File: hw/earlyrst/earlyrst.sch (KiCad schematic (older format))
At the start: 13 parts

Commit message: comment about -pcLoad signal
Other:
- note added: "-pcLoad asserts the initial PC\nupper/lower byte value on the\nALU data bus, and also drives\nthe parallel load input on the\nPC register"
- note removed: "-pcLoad asserts the initial PC\nupper/lower byte value on the\nALU data bus"
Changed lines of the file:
@@
 	1    0    0    -1
 $EndComp
-Text Notes 9700 1350 0    60   ~ 0
--pcLoad asserts the initial PC\nupper/lower byte value on the\nALU data bus
+Text Notes 9550 1300 0    60   ~ 0
+-pcLoad asserts the initial PC\nupper/lower byte value on the\nALU data bus, and also drives\nthe parallel load input on the\nPC register
 Text Notes 9850 3150 0    60   ~ 0
 -lateRST is the active-low\nreset signal for all other\ndevices

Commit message: bugfix/redesign
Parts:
- removed U?: 74LS32, symbol 74LS32
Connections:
- wire segments 83 -> 77
- no-connect marks 8 -> 7
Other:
- note added: "-lateRST is the\nactive-low reset\nsignal for all other\ndevices"
- note added: "-pcLoad asserts the initial PC\nupper/lower byte value on the\nALU data bus"
- note removed: "-lateRST is the active-low\nreset signal for all other\ndevices"
- note removed: "-pcLoad asserts the initial PC\nupper/lower byte value on the\nALU data bus, and also drives\nthe parallel load input on the\nPC register"
- moved on the sheet: U?, U?A, U?B, U?C, U?D
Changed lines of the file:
@@
 L 74LS32 U?
 U 1 1 592592CC
-P 5850 2600
-F 0 "U?" H 5850 2650 50  0000 C CNN
-F 1 "74LS32" H 5850 2550 50  0000 C CNN
-F 2 "" H 5850 2600 50  0001 C CNN
-F 3 "" H 5850 2600 50  0001 C CNN
-	1    5850 2600
+P 6750 2600
+F 0 "U?" H 6750 2650 50  0000 C CNN
+F 1 "74LS32" H 6750 2550 50  0000 C CNN
+F 2 "" H 6750 2600 50  0001 C CNN
+F 3 "" H 6750 2600 50  0001 C CNN
+	1    6750 2600
 	1    0    0    -1
 $EndComp
@@
 L 74LS04 U?
 U 3 1 59259341
-P 7050 2600
-F 0 "U?" H 7245 2715 50  0000 C CNN
-F 1 "74LS04" H 7240 2475 50  0000 C CNN
-F 2 "" H 7050 2600 50  0001 C CNN
-F 3 "" H 7050 2600 50  0001 C CNN
-	3    7050 2600
+P 5550 2500
+F 0 "U?" H 5745 2615 50  0000 C CNN
+F 1 "74LS04" H 5740 2375 50  0000 C CNN
+F 2 "" H 5550 2500 50  0001 C CNN
+F 3 "" H 5550 2500 50  0001 C CNN
+	3    5550 2500
 	1    0    0    -1
 $EndComp
@@
 L 74LS175 U?
 U 1 1 59259407
-P 8350 3050
-F 0 "U?" H 8350 3050 50  0000 C CNN
-F 1 "74LS175" H 8450 2650 50  0000 C CNN
-F 2 "" H 8350 3050 50  0001 C CNN
-F 3 "" H 8350 3050 50  0001 C CNN
-	1    8350 3050
+P 8550 3050
+F 0 "U?" H 8550 3050 50  0000 C CNN
+F 1 "74LS175" H 8650 2650 50  0000 C CNN
+F 2 "" H 8550 3050 50  0001 C CNN
+F 3 "" H 8550 3050 50  0001 C CNN
+	1    8550 3050
 	1    0    0    -1
 $EndComp
@@
 L 74LS32 U?
 U 2 1 59259471
-P 5850 3350
-F 0 "U?" H 5850 3400 50  0000 C CNN
-F 1 "74LS32" H 5850 3300 50  0000 C CNN
-F 2 "" H 5850 3350 50  0001 C CNN
-F 3 "" H 5850 3350 50  0001 C CNN
-	2    5850 3350
-	1    0    0    -1
-$EndComp
-Text Label 4650 2500 0    60   ~ 0
-CT0
-Text Label 4650 2600 0    60   ~ 0
-CT1
-Text Label 9900 2800 0    60   ~ 0
+P 6750 3100
+F 0 "U?" H 6750 3150 50  0000 C CNN
+F 1 "74LS32" H 6750 3050 50  0000 C CNN
+F 2 "" H 6750 3100 50  0001 C CNN
+F 3 "" H 6750 3100 50  0001 C CNN
+	2    6750 3100
+	1    0    0    -1
+$EndComp
+Text Label 10100 2800 0    60   ~ 0
 -lateRST
 $Comp
 L GND #PWR?
 U 1 1 59259887
-P 6800 3500
-F 0 "#PWR?" H 6800 3250 50  0001 C CNN
-F 1 "GND" H 6800 3350 50  0000 C CNN
-F 2 "" H 6800 3500 50  0001 C CNN
-F 3 "" H 6800 3500 50  0001 C CNN
-	1    6800 3500
+P 7700 4500
+F 0 "#PWR?" H 7700 4250 50  0001 C CNN
+F 1 "GND" H 7700 4350 50  0000 C CNN
+F 2 "" H 7700 4500 50  0001 C CNN
+F 3 "" H 7700 4500 50  0001 C CNN
+	1    7700 4500
 	1    0    0    -1
 $EndComp
@@
 $Comp
 L 74LS32 U?
-U 3 1 59259CFD
-P 10050 1600
-F 0 "U?" H 10050 1650 50  0000 C CNN
-F 1 "74LS32" H 10050 1550 50  0000 C CNN
-F 2 "" H 10050 1600 50  0001 C CNN
-F 3 "" H 10050 1600 50  0001 C CNN
-	3    10050 1600
-	1    0    0    -1
-$EndComp
-Text Label 10700 1600 0    60   ~ 0
--pcLoad
-$Comp
-L 74LS32 U?
 U 4 1 5925A3F5
 P 2900 5500
@@
 L 74LS04 U?
 U 4 1 5925A468
-P 2750 5950
-F 0 "U?" H 2945 6065 50  0000 C CNN
-F 1 "74LS04" H 2940 5825 50  0000 C CNN
-F 2 "" H 2750 5950 50  0001 C CNN
-F 3 "" H 2750 5950 50  0001 C CNN
-	4    2750 5950
+P 5550 3000
+F 0 "U?" H 5745 3115 50  0000 C CNN
+F 1 "74LS04" H 5740 2875 50  0000 C CNN
+F 2 "" H 5550 3000 50  0001 C CNN
+F 3 "" H 5550 3000 50  0001 C CNN
+	4    5550 3000
 	1    0    0    -1
 $EndComp
@@
 	1    0    0    -1
 $EndComp
-Text Notes 9550 1300 0    60   ~ 0
--pcLoad asserts the initial PC\nupper/lower byte value on the\nALU data bus, and also drives\nthe parallel load input on the\nPC register
-Text Notes 9850 3150 0    60   ~ 0
--lateRST is the active-low\nreset signal for all other\ndevices
+Text Notes 10050 3250 0    60   ~ 0
+-lateRST is the\nactive-low reset\nsignal for all other\ndevices
 $Comp
 L GND #PWR?
@@
 $EndComp
 NoConn ~ 3750 5500
-NoConn ~ 3750 5950
 NoConn ~ 3750 6300
 NoConn ~ 3750 6650
@@
 	4600 2700 4900 2700
 Wire Wire Line
-	6600 2600 6450 2600
-Wire Wire Line
-	5250 2700 5100 2700
-Wire Wire Line
-	5100 2600 5100 3250
-Wire Wire Line
-	5100 3250 5250 3250
-Connection ~ 5100 2700
-Wire Wire Line
-	4600 2500 5250 2500
-Wire Wire Line
-	4600 2600 5100 2600
-Wire Wire Line
-	7500 2600 7650 2600
-Wire Wire Line
-	9050 2800 10400 2800
-Wire Wire Line
-	5250 3450 5100 3450
-Wire Wire Line
-	5100 3450 5100 3850
-Wire Wire Line
-	5100 3850 9650 3850
-Wire Wire Line
-	9650 3850 9650 2800
-Connection ~ 9650 2800
-Wire Wire Line
-	7650 2800 7350 2800
-Wire Wire Line
-	7350 2800 7350 3350
-Wire Wire Line
-	7350 3350 6450 3350
-Wire Wire Line
-	7650 3000 6800 3000
-Wire Wire Line
-	6800 3000 6800 3500
-Wire Wire Line
-	7650 3200 6800 3200
-Connection ~ 6800 3200
-Wire Wire Line
-	7650 3500 7550 3500
-Wire Wire Line
-	7550 3500 7550 4300
-Wire Wire Line
-	7550 4300 750  4300
+	7350 2600 7850 2600
+Wire Wire Line
+	9250 2800 10600 2800
+Wire Wire Line
+	9850 3850 9850 2800
+Connection ~ 9850 2800
+Wire Wire Line
+	750  4300 7550 4300
 Connection ~ 750  3300
 Wire Wire Line
-	9300 1500 9300 2700
-Wire Wire Line
 	1000 1050 550  1050
 Wire Wire Line
 	750  1400 550  1400
 Wire Wire Line
-	7650 3400 7450 3400
-Wire Wire Line
-	7450 3400 7450 4150
-Wire Wire Line
-	7450 4150 1000 4150
+	1000 4150 7450 4150
 Connection ~ 1000 2950
-Wire Wire Line
-	9450 1700 9450 2800
-Connection ~ 9450 2800
-Wire Wire Line
-	9300 1500 9450 1500
-Wire Wire Line
-	10650 1600 11100 1600
 Wire Wire Line
 	2300 5400 1900 5400
@@
 Connection ~ 1900 5600
 Wire Wire Line
-	2300 5950 1900 5950
-Connection ~ 1900 5950
-Wire Wire Line
 	2300 6300 1900 6300
 Connection ~ 1900 6300
@@
 	3500 5500 3750 5500
 Wire Wire Line
-	3200 5950 3750 5950
-Wire Wire Line
 	3200 6300 3750 6300
 Wire Wire Line
 	3200 6650 3750 6650
-Wire Wire Line
-	9300 2700 9050 2700
 Wire Wire Line
 	6100 5600 4950 5600
@@
 Text Notes 6350 6300 0    60   ~ 0
 the initial PC value is\n0xC0C0
+Wire Wire Line
+	9250 2600 10600 2600
+Text Label 10100 2600 0    60   ~ 0
+-pcLoad
+Wire Wire Line
+	6150 2500 6000 2500
+Wire Wire Line
+	7850 3000 7700 3000
+Wire Wire Line
+	7700 3000 7700 4500
+Wire Wire Line
+	7850 3200 7700 3200
+Connection ~ 7700 3200
+Wire Wire Line
+	4600 2500 5100 2500
+Wire Wire Line
+	4600 2600 5100 2600
+Wire Wire Line
+	5100 2600 5100 3000
+Text Label 4600 2500 0    60   ~ 0
+CT0
+Text Label 4600 2600 0    60   ~ 0
+CT1
+Wire Wire Line
+	6000 3000 6150 3000
+Wire Wire Line
+	7850 3500 7550 3500
+Wire Wire Line
+	7550 3500 7550 4300
+Wire Wire Line
+	7850 3400 7450 3400
+Wire Wire Line
+	7450 3400 7450 4150
+Wire Wire Line
+	9850 3850 6050 3850
+Wire Wire Line
+	6050 3850 6050 2700
+Wire Wire Line
+	6050 2700 6150 2700
+Wire Wire Line
+	6150 3200 6050 3200
+Connection ~ 6050 3200
+Wire Wire Line
+	7350 3100 7500 3100
+Wire Wire Line
+	7500 3100 7500 2800
+Wire Wire Line
+	7500 2800 7850 2800
+Text Notes 9600 2450 0    60   ~ 0
+-pcLoad asserts the initial PC\nupper/lower byte value on the\nALU data bus
 $EndSCHEMATC

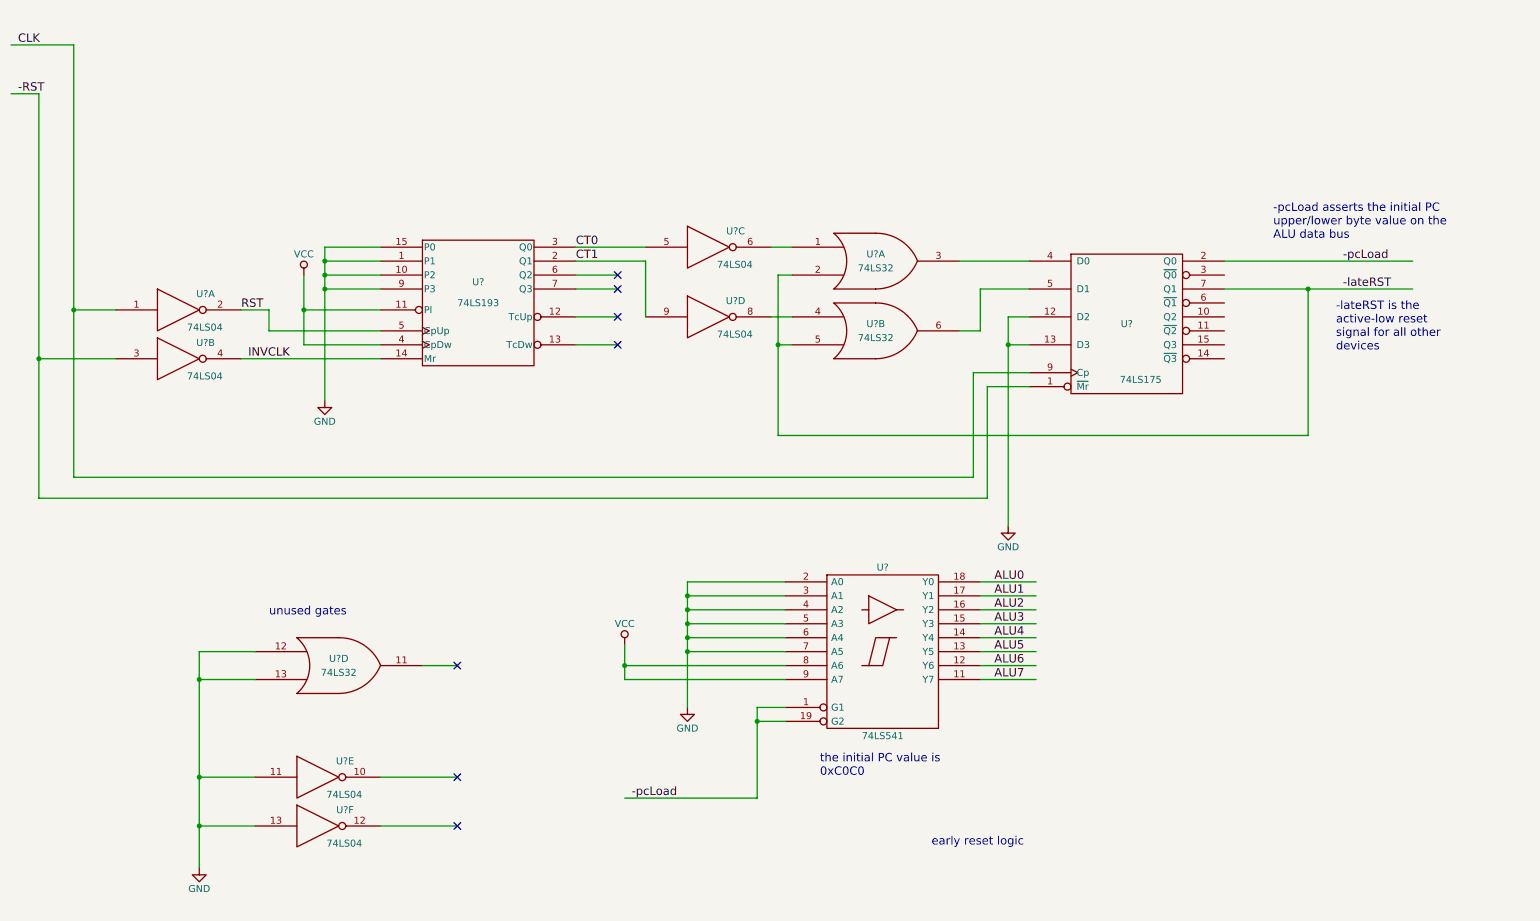
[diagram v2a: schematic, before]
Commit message: annotate schematic, note unused or gate
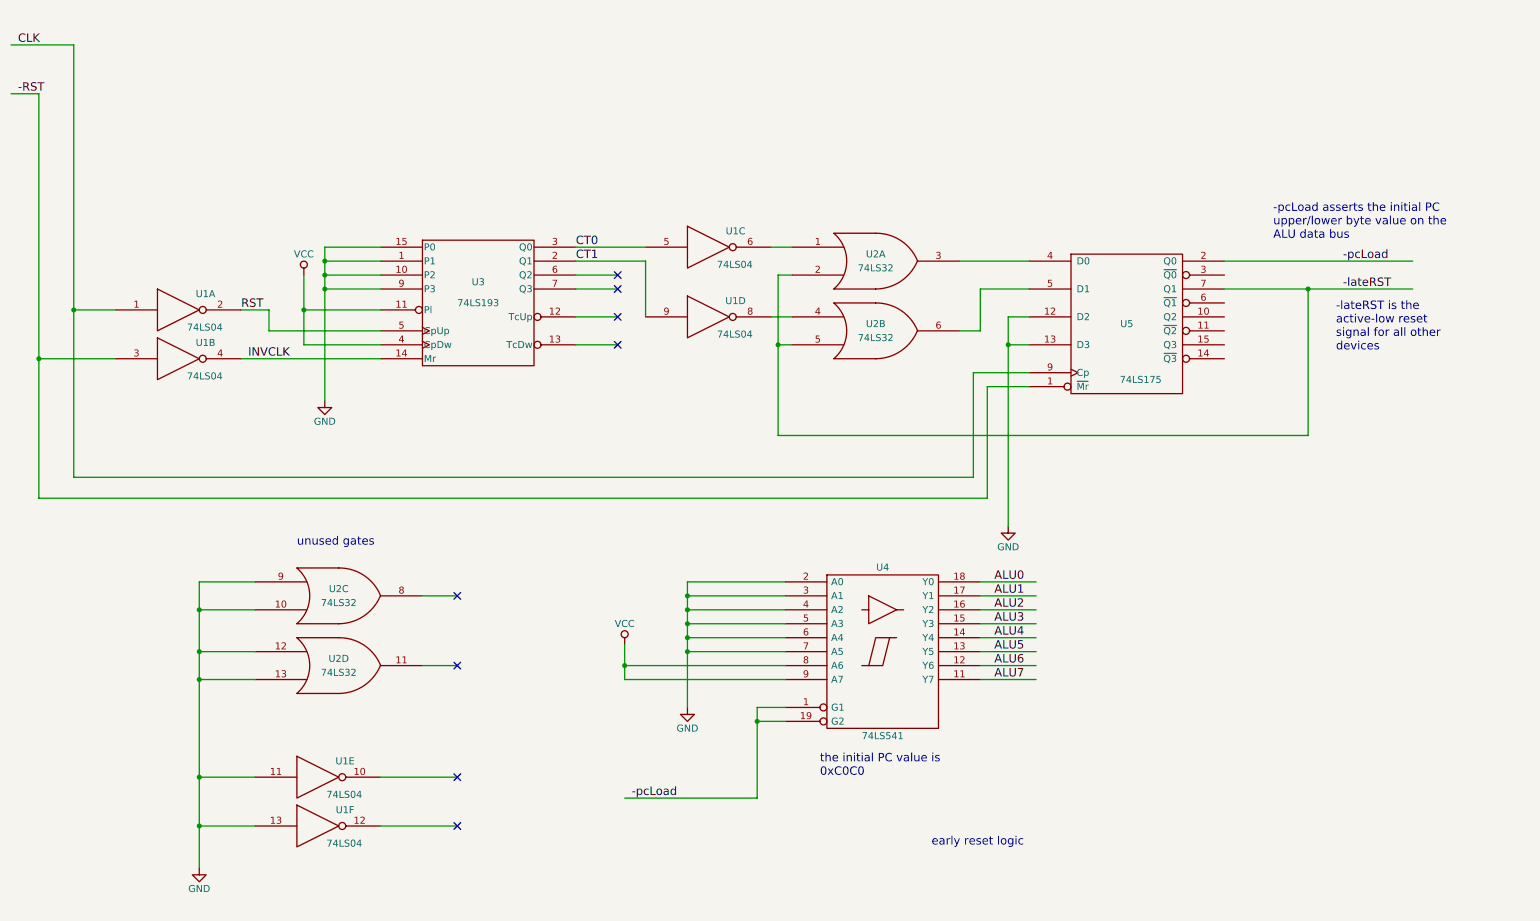
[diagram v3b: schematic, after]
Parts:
- added unit 1 of U2
- gave numbers to parts that had none: 5
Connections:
- wire segments 77 -> 80
- no-connect marks 7 -> 8
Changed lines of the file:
@@
 LIBS:contrib
 LIBS:valves
+LIBS:earlyrst-cache
 EELAYER 25 0
 EELAYER END
@@
 early reset logic
 $Comp
-L 74LS193 U?
+L 74LS193 U3
 U 1 1 59258F23
 P 3900 2900
-F 0 "U?" H 3900 3050 50  0000 C CNN
+F 0 "U3" H 3900 3050 50  0000 C CNN
 F 1 "74LS193" H 3900 2900 50  0000 C CNN
 F 2 "" H 3900 2900 50  0001 C CNN
@@
 $EndComp
 $Comp
-L 74LS04 U?
+L 74LS04 U1
 U 1 1 59258F5A
 P 1750 2950
-F 0 "U?" H 1945 3065 50  0000 C CNN
+F 0 "U1" H 1945 3065 50  0000 C CNN
 F 1 "74LS04" H 1940 2825 50  0000 C CNN
 F 2 "" H 1750 2950 50  0001 C CNN
@@
 $EndComp
 $Comp
-L 74LS04 U?
+L 74LS04 U1
 U 2 1 59258FEB
 P 1750 3300
-F 0 "U?" H 1945 3415 50  0000 C CNN
+F 0 "U1" H 1945 3415 50  0000 C CNN
 F 1 "74LS04" H 1940 3175 50  0000 C CNN
 F 2 "" H 1750 3300 50  0001 C CNN
@@
 $EndComp
 $Comp
-L VCC #PWR?
+L VCC #PWR2
 U 1 1 592590E2
 P 2650 2700
-F 0 "#PWR?" H 2650 2550 50  0001 C CNN
+F 0 "#PWR2" H 2650 2550 50  0001 C CNN
 F 1 "VCC" H 2650 2850 50  0000 C CNN
 F 2 "" H 2650 2700 50  0001 C CNN
@@
 $EndComp
 $Comp
-L GND #PWR?
+L GND #PWR3
 U 1 1 5925914D
 P 2800 3600
-F 0 "#PWR?" H 2800 3350 50  0001 C CNN
+F 0 "#PWR3" H 2800 3350 50  0001 C CNN
 F 1 "GND" H 2800 3450 50  0000 C CNN
 F 2 "" H 2800 3600 50  0001 C CNN
@@
 NoConn ~ 4900 2800
 $Comp
-L 74LS32 U?
-U 1 1 592592CC
-P 6750 2600
-F 0 "U?" H 6750 2650 50  0000 C CNN
-F 1 "74LS32" H 6750 2550 50  0000 C CNN
-F 2 "" H 6750 2600 50  0001 C CNN
-F 3 "" H 6750 2600 50  0001 C CNN
-	1    6750 2600
-	1    0    0    -1
-$EndComp
-$Comp
-L 74LS04 U?
-U 3 1 59259341
-P 5550 2500
-F 0 "U?" H 5745 2615 50  0000 C CNN
-F 1 "74LS04" H 5740 2375 50  0000 C CNN
-F 2 "" H 5550 2500 50  0001 C CNN
-F 3 "" H 5550 2500 50  0001 C CNN
-	3    5550 2500
-	1    0    0    -1
-$EndComp
-$Comp
-L 74LS175 U?
+L 74LS32 U2
+U 3 1 592592CC
+P 2900 5000
+F 0 "U2" H 2900 5050 50  0000 C CNN
+F 1 "74LS32" H 2900 4950 50  0000 C CNN
+F 2 "" H 2900 5000 50  0001 C CNN
+F 3 "" H 2900 5000 50  0001 C CNN
+	3    2900 5000
+	1    0    0    -1
+$EndComp
+$Comp
+L 74LS04 U1
+U 5 1 59259341
+P 2750 6300
+F 0 "U1" H 2945 6415 50  0000 C CNN
+F 1 "74LS04" H 2940 6175 50  0000 C CNN
+F 2 "" H 2750 6300 50  0001 C CNN
+F 3 "" H 2750 6300 50  0001 C CNN
+	5    2750 6300
+	1    0    0    -1
+$EndComp
+$Comp
+L 74LS175 U5
 U 1 1 59259407
 P 8550 3050
-F 0 "U?" H 8550 3050 50  0000 C CNN
+F 0 "U5" H 8550 3050 50  0000 C CNN
 F 1 "74LS175" H 8650 2650 50  0000 C CNN
 F 2 "" H 8550 3050 50  0001 C CNN
@@
 $EndComp
 $Comp
-L 74LS32 U?
-U 2 1 59259471
-P 6750 3100
-F 0 "U?" H 6750 3150 50  0000 C CNN
-F 1 "74LS32" H 6750 3050 50  0000 C CNN
-F 2 "" H 6750 3100 50  0001 C CNN
-F 3 "" H 6750 3100 50  0001 C CNN
-	2    6750 3100
+L 74LS32 U2
+U 4 1 59259471
+P 2900 5500
+F 0 "U2" H 2900 5550 50  0000 C CNN
+F 1 "74LS32" H 2900 5450 50  0000 C CNN
+F 2 "" H 2900 5500 50  0001 C CNN
+F 3 "" H 2900 5500 50  0001 C CNN
+	4    2900 5500
 	1    0    0    -1
 $EndComp
@@
 -lateRST
 $Comp
-L GND #PWR?
+L GND #PWR6
 U 1 1 59259887
 P 7700 4500
-F 0 "#PWR?" H 7700 4250 50  0001 C CNN
+F 0 "#PWR6" H 7700 4250 50  0001 C CNN
 F 1 "GND" H 7700 4350 50  0000 C CNN
 F 2 "" H 7700 4500 50  0001 C CNN
@@
 INVCLK
 $Comp
-L 74LS32 U?
-U 4 1 5925A3F5
-P 2900 5500
-F 0 "U?" H 2900 5550 50  0000 C CNN
-F 1 "74LS32" H 2900 5450 50  0000 C CNN
-F 2 "" H 2900 5500 50  0001 C CNN
-F 3 "" H 2900 5500 50  0001 C CNN
-	4    2900 5500
-	1    0    0    -1
-$EndComp
-$Comp
-L 74LS04 U?
-U 4 1 5925A468
+L 74LS32 U2
+U 2 1 5925A3F5
+P 6750 3100
+F 0 "U2" H 6750 3150 50  0000 C CNN
+F 1 "74LS32" H 6750 3050 50  0000 C CNN
+F 2 "" H 6750 3100 50  0001 C CNN
+F 3 "" H 6750 3100 50  0001 C CNN
+	2    6750 3100
+	1    0    0    -1
+$EndComp
+$Comp
+L 74LS04 U1
+U 6 1 5925A468
+P 2750 6650
+F 0 "U1" H 2945 6765 50  0000 C CNN
+F 1 "74LS04" H 2940 6525 50  0000 C CNN
+F 2 "" H 2750 6650 50  0001 C CNN
+F 3 "" H 2750 6650 50  0001 C CNN
+	6    2750 6650
+	1    0    0    -1
+$EndComp
+$Comp
+L 74LS04 U1
+U 3 1 5925A4A5
+P 5550 2500
+F 0 "U1" H 5745 2615 50  0000 C CNN
+F 1 "74LS04" H 5740 2375 50  0000 C CNN
+F 2 "" H 5550 2500 50  0001 C CNN
+F 3 "" H 5550 2500 50  0001 C CNN
+	3    5550 2500
+	1    0    0    -1
+$EndComp
+$Comp
+L 74LS04 U1
+U 4 1 5925A4D4
 P 5550 3000
-F 0 "U?" H 5745 3115 50  0000 C CNN
+F 0 "U1" H 5745 3115 50  0000 C CNN
 F 1 "74LS04" H 5740 2875 50  0000 C CNN
 F 2 "" H 5550 3000 50  0001 C CNN
@@
 	1    0    0    -1
 $EndComp
-$Comp
-L 74LS04 U?
-U 5 1 5925A4A5
-P 2750 6300
-F 0 "U?" H 2945 6415 50  0000 C CNN
-F 1 "74LS04" H 2940 6175 50  0000 C CNN
-F 2 "" H 2750 6300 50  0001 C CNN
-F 3 "" H 2750 6300 50  0001 C CNN
-	5    2750 6300
-	1    0    0    -1
-$EndComp
-$Comp
-L 74LS04 U?
-U 6 1 5925A4D4
-P 2750 6650
-F 0 "U?" H 2945 6765 50  0000 C CNN
-F 1 "74LS04" H 2940 6525 50  0000 C CNN
-F 2 "" H 2750 6650 50  0001 C CNN
-F 3 "" H 2750 6650 50  0001 C CNN
-	6    2750 6650
-	1    0    0    -1
-$EndComp
 Text Notes 10050 3250 0    60   ~ 0
 -lateRST is the\nactive-low reset\nsignal for all other\ndevices
 $Comp
-L GND #PWR?
+L GND #PWR1
 U 1 1 5925AADF
 P 1900 6950
-F 0 "#PWR?" H 1900 6700 50  0001 C CNN
+F 0 "#PWR1" H 1900 6700 50  0001 C CNN
 F 1 "GND" H 1900 6800 50  0000 C CNN
 F 2 "" H 1900 6950 50  0001 C CNN
@@
 NoConn ~ 3750 6300
 NoConn ~ 3750 6650
-Text Notes 2400 5150 0    60   ~ 0
+Text Notes 2600 4650 0    60   ~ 0
 unused gates
 $Comp
-L 74LS541 U?
+L 74LS541 U4
 U 1 1 5925B1A9
 P 6800 5400
-F 0 "U?" H 6800 5975 50  0000 C BNN
+F 0 "U4" H 6800 5975 50  0000 C BNN
 F 1 "74LS541" H 6800 4825 50  0000 C TNN
 F 2 "" H 6800 5400 50  0001 C CNN
@@
 $EndComp
 $Comp
-L VCC #PWR?
+L VCC #PWR4
 U 1 1 5925B2D7
 P 4950 5350
-F 0 "#PWR?" H 4950 5200 50  0001 C CNN
+F 0 "#PWR4" H 4950 5200 50  0001 C CNN
 F 1 "VCC" H 4950 5500 50  0000 C CNN
 F 2 "" H 4950 5350 50  0001 C CNN
@@
 	2300 5400 1900 5400
 Wire Wire Line
-	1900 5400 1900 6950
+	1900 4900 1900 6950
 Wire Wire Line
 	2300 5600 1900 5600
@@
 Connection ~ 5400 5400
 $Comp
-L GND #PWR?
+L GND #PWR5
 U 1 1 5925B869
 P 5400 5800
-F 0 "#PWR?" H 5400 5550 50  0001 C CNN
+F 0 "#PWR5" H 5400 5550 50  0001 C CNN
 F 1 "GND" H 5400 5650 50  0000 C CNN
 F 2 "" H 5400 5800 50  0001 C CNN
@@
 Text Notes 9600 2450 0    60   ~ 0
 -pcLoad asserts the initial PC\nupper/lower byte value on the\nALU data bus
+$Comp
+L 74LS32 U2
+U 1 1 5926DE4E
+P 6750 2600
+F 0 "U2" H 6750 2650 50  0000 C CNN
+F 1 "74LS32" H 6750 2550 50  0000 C CNN
+F 2 "" H 6750 2600 50  0001 C CNN
+F 3 "" H 6750 2600 50  0001 C CNN
+	1    6750 2600
+	1    0    0    -1
+$EndComp
+Wire Wire Line
+	2300 4900 1900 4900
+Connection ~ 1900 5400
+Wire Wire Line
+	2300 5100 1900 5100
+Connection ~ 1900 5100
+NoConn ~ 3750 5000
+Wire Wire Line
+	3500 5000 3750 5000
 $EndSCHEMATC
